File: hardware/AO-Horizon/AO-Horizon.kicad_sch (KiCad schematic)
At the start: 0 parts

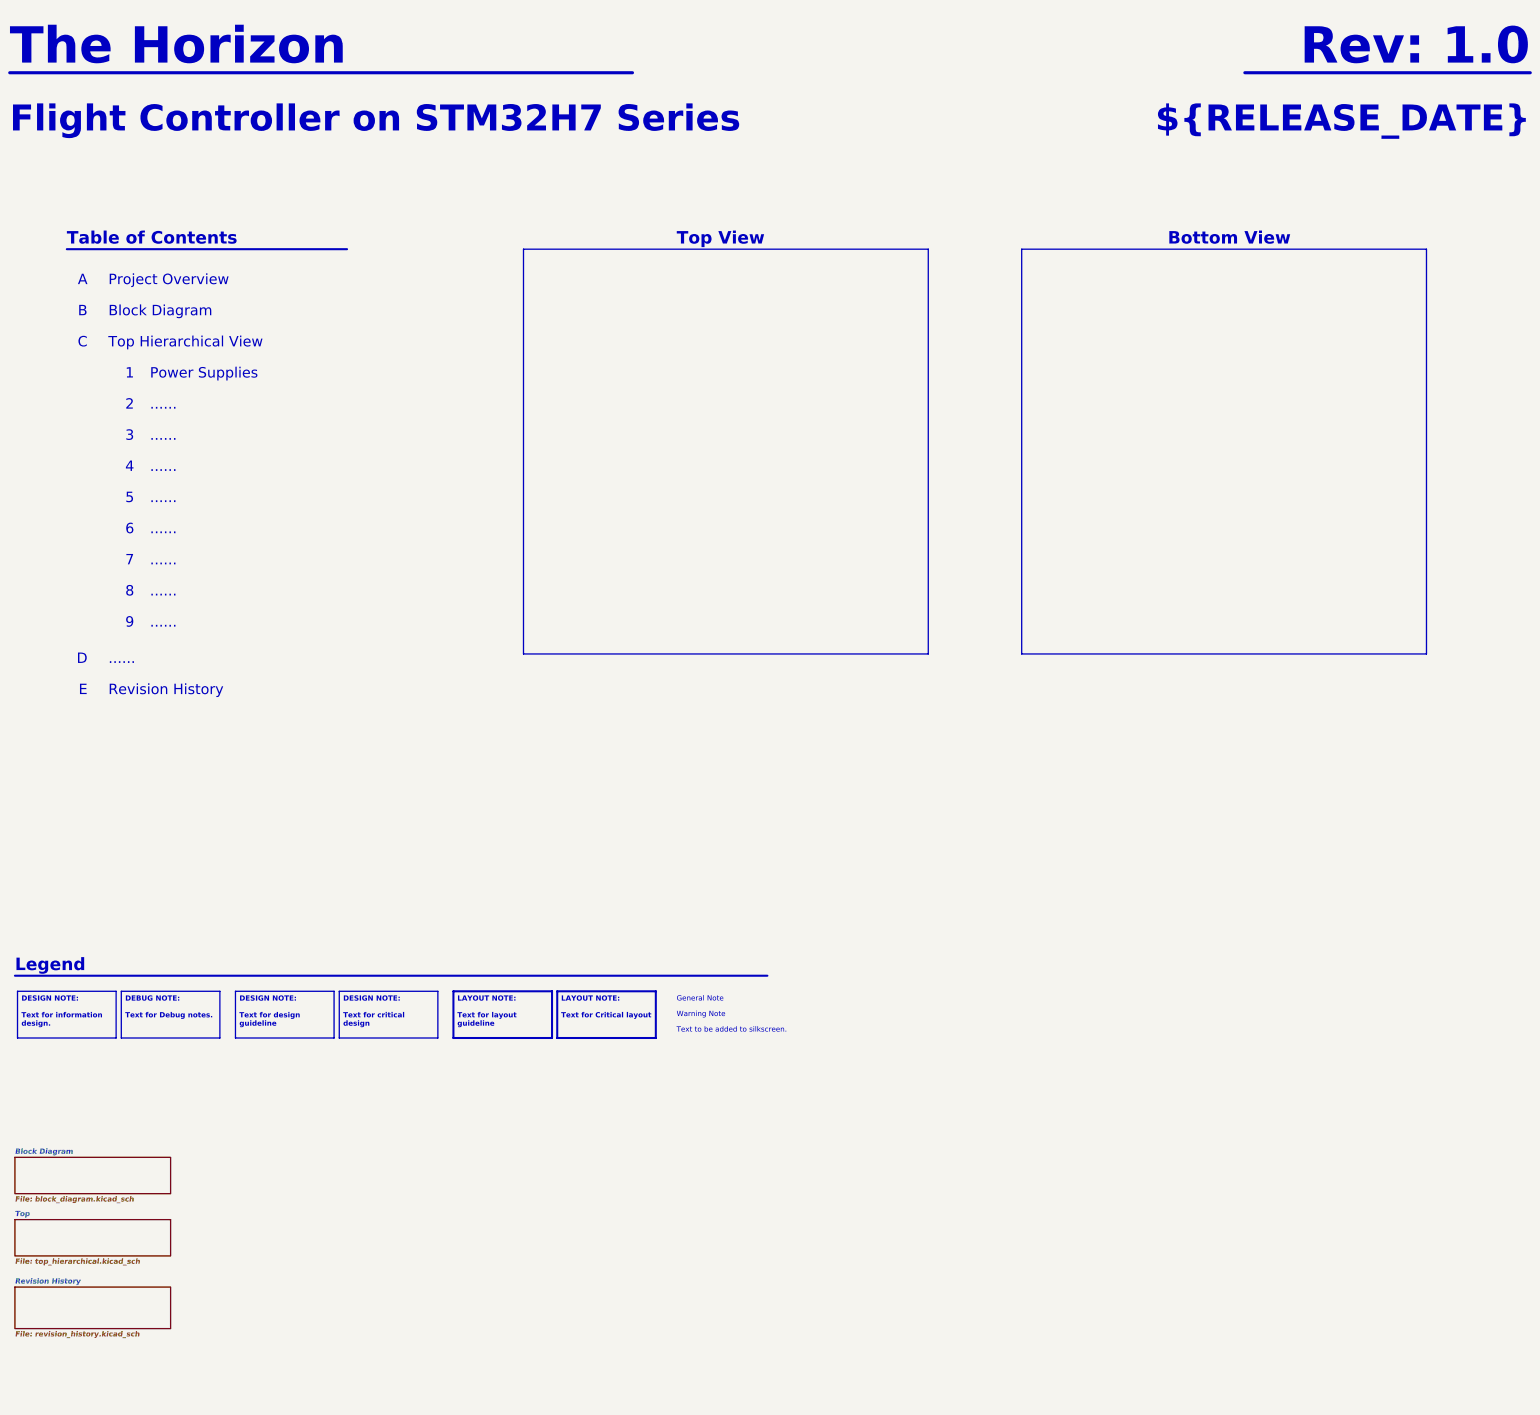
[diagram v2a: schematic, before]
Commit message: feat: close the power sheet capture (spec 0.19, DEC-027, DEC-028) (#31)
* docs(readme): simplify workflow diagram explanation

Mark DRAFT as under review, sync CHECK label, and add a colour key in README and template.

Co-Authored-By: Claude Sonnet 5.5 <noreply@anthropic.com>

* Update settings.json

* change spec file name

* update git-workflow skill

* change skill name by add hw-*

* docs: update AeroOptix-Horizon hardware spec

* docs: consolidate hardware handoff into checklist

* Update CLAUDE.md

* Update CLAUDE.md

* Update CLAUDE.md

* feat(hooks): replace protect hook with rule-based v2

Move file-protection rules into hooks/protect.json (allow > deny > ask)
and use ask for editable-with-approval files instead of a hard block.
Bash/PowerShell checks now inspect write targets, not any mention of a
protected path. Align settings.json permissions and drop the old hook.

Co-Authored-By: Claude Sonnet 5.5 <noreply@anthropic.com>

* docs: update CLAUDE.md for protection tiers and skill names

Describe the ask/deny protection rules, the v2 hook and protect.json,
and fix stale skill and template names.

Co-Authored-By: Claude Sonnet 5.5 <noreply@anthropic.com>

* Update .gitignore

* Update .gitignore

* Update .gitignore

* del skills

* Update engineering.md

* Update git-workflow.md

* Update hardware-workflow.md

* Update settings.json

* Update pull_request_template.md

* Update .gitignore

* Update .gitignore

* Delete SKILL.md

* Delete SKILL.md

* Update .gitignore

* add git-workflow skill

* Update CLAUDE.md

* Update protect.json

* Update settings.json

* Create MEMORY.md

* feat(agents): add codex-hw-delegate for bounded Codex tasks

Add a project agent that delegates one small, read-only-by-default task
to Codex CLI. It gates trivial or ambiguous requests, refuses PDF and
KiCad file contents, never mutates git, cross-checks Codex output and
returns a fixed report format.

Co-Authored-By: Claude Sonnet 5.5 <noreply@anthropic.com>

* fix(hooks): resol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
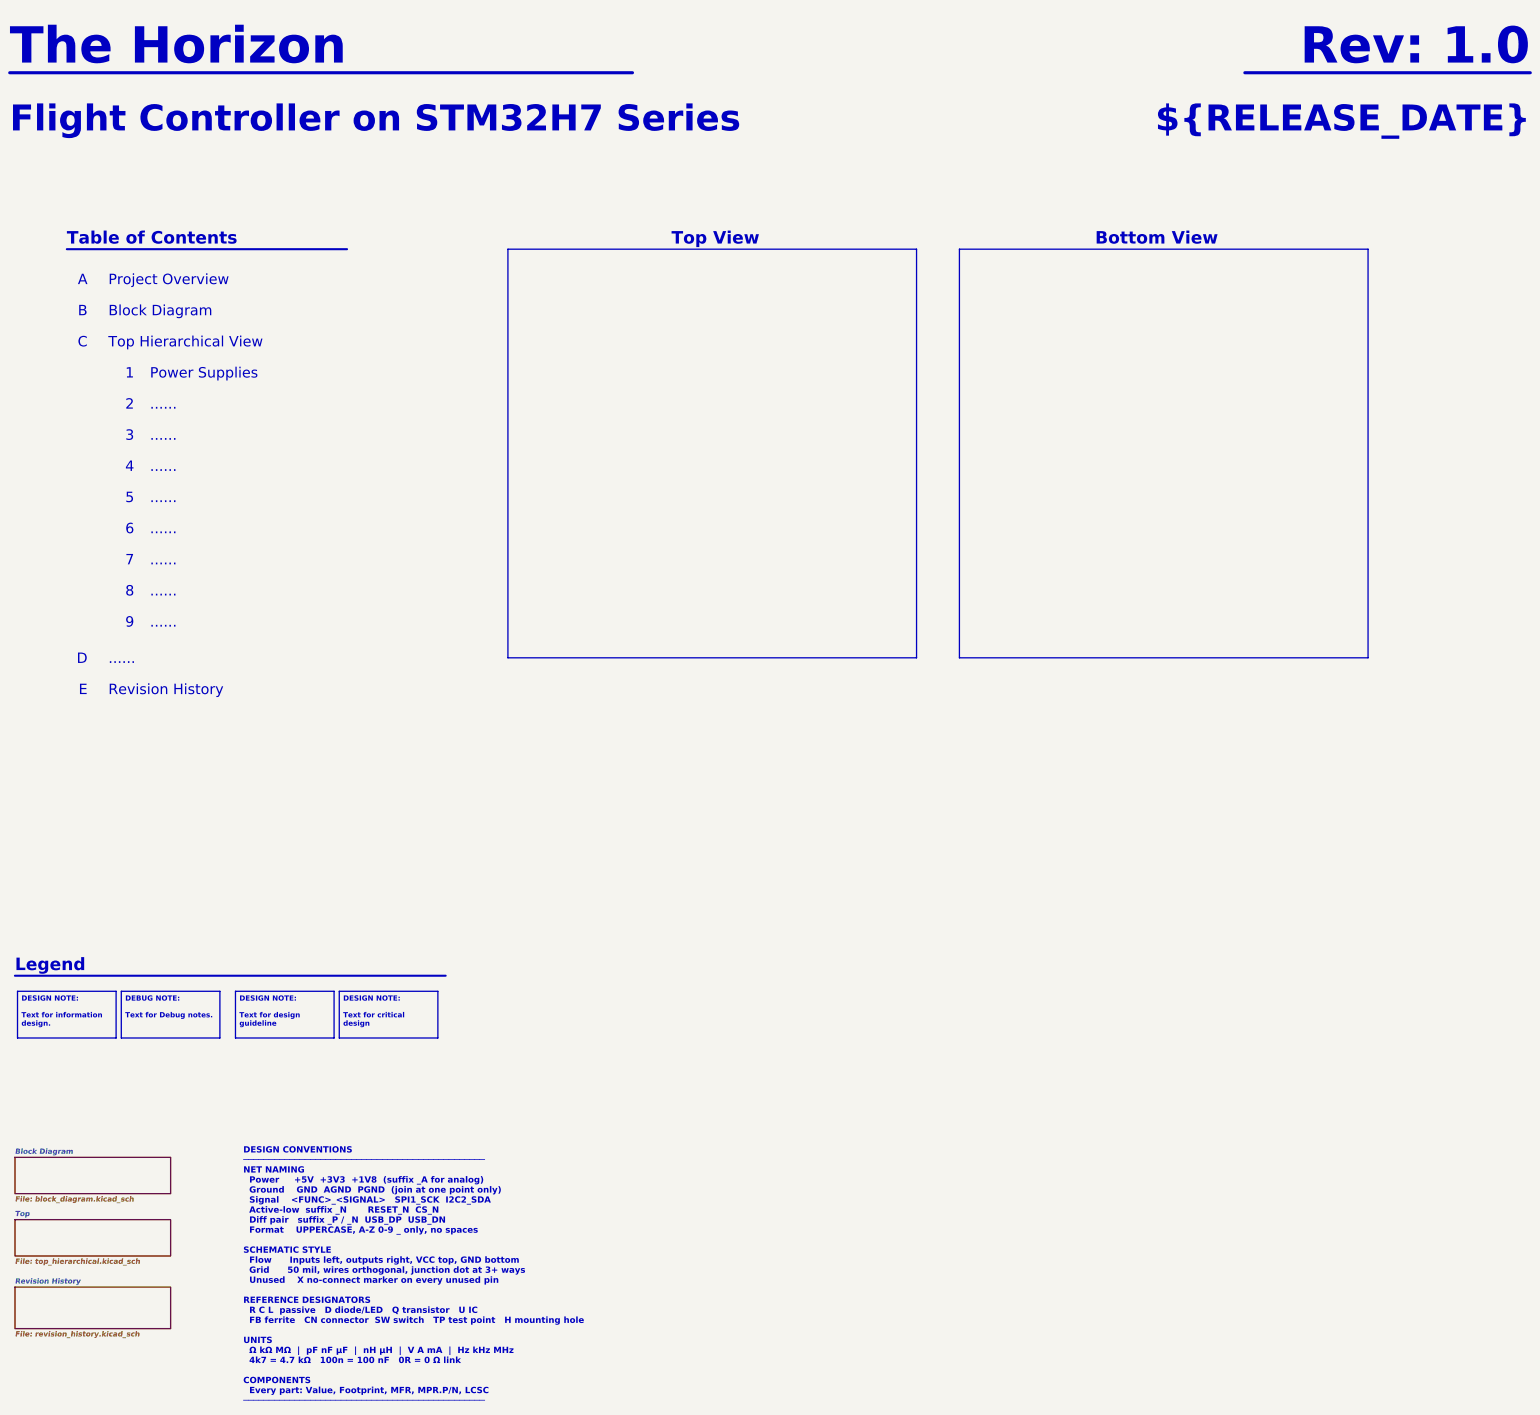
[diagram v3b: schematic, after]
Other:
- note added: "DESIGN CONVENTIONS ─────────────────────────────────────────────── NET NAMING Power +5V +3V3 +1V8 (suffix _A for analog) Ground GND AGND PGND (join at one point only) Signal <FUNC>_<SIGNAL> SPI1_SCK I2C2_SDA Active-low suffix _N RESET_N CS_N Diff pair suffix _P / _N USB_DP USB_DN Format UPPERCASE, A-Z 0-9 _ only, no spaces SCHEMATIC STYLE Flow Inputs left, outputs right, VCC top, GND bottom Grid 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"
- note removed: "General Note"
- note removed: "Text to be added to silkscreen."
- note removed: "Warning Note"
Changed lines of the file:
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@@
 	)
 	(rectangle
-		(start 151.13 83.82)
-		(end 250.19 182.88)
+		(start 147.32 83.82)
+		(end 247.32 183.82)
 		(stroke
 			(width 0)
@@
 	)
 	(rectangle
-		(start 273.05 83.82)
-		(end 372.11 182.88)
+		(start 257.81 83.82)
+		(end 357.81 183.82)
 		(stroke
 			(width 0)
@@
 		)
 	)
+	(text "DESIGN CONVENTIONS\n───────────────────────────────────────────────\nNET NAMING\n  Power     +5V  +3V3  +1V8  (suffix _A for analog)\n  Ground    GND  AGND  PGND  (join at one point only)\n  Signal    <FUNC>_<SIGNAL>   SPI1_SCK  I2C2_SDA\n  Active-low  suffix _N       RESET_N  CS_N\n  Diff pair   suffix _P / _N  USB_DP  USB_DN\n  Format    UPPERCASE, A-Z 0-9 _ only, no spaces\n\nSCHEMATIC STYLE\n  Flow      Inputs left, outputs right, VCC top, GND bottom\n  Grid      50 mil, wires orthogonal, junction dot at 3+ ways\n  Unused    X no-connect marker on every unused pin\n\nREFERENCE DESIGNATORS\n  R C L  passive   D diode/LED   Q transistor   U IC\n  FB ferrite   CN connector  SW switch   TP test point   H mounting hole\n\nUNITS\n  Ω kΩ MΩ  |  pF nF µF  |  nH µH  |  V A mA  |  Hz kHz MHz\n  4k7 = 4.7 kΩ   100n = 100 nF   0R = 0 Ω link\n\nCOMPONENTS\n  Every part: Value, Footprint, MFR, MPR.P/N, LCSC\n───────────────────────────────────────────────"
+		(exclude_from_sim no)
+		(at 82.55 303.53 0)
+		(effects
+			(font
+				(face "Century Gothic")
+				(size 1.524 1.524)
+				(bold yes)
+			)
+			(justify left top)
+		)
+	)
 	(text "......"
 		(exclude_from_sim no)
@@
 		)
 	)
-	(text "General Note"
-		(exclude_from_sim no)
-		(at 188.595 267.335 0)
-		(effects
-			(font
-				(size 1.27 1.27)
-				(color 0 0 194 1)
-			)
-			(justify left)
-		)
-	)
 	(text "Project Overview"
 		(exclude_from_sim no)
@@
 		)
 	)
-	(text "Text to be added to silkscreen."
-		(exclude_from_sim no)
-		(at 188.595 274.955 0)
-		(effects
-			(font
-				(size 1.27 1.27)
-				(color 0 132 132 1)
-			)
-			(justify left)
-		)
-	)
 	(text "6"
 		(exclude_from_sim no)
@@
 		)
 	)
-	(text "Warning Note"
-		(exclude_from_sim no)
-		(at 188.595 271.145 0)
-		(effects
-			(font
-				(size 1.27 1.27)
-				(color 194 0 0 1)
-			)
-			(justify left)
-		)
-	)
 	(text "Table of Contents"
 		(exclude_from_sim no)
@@
 	(text "Bottom View"
 		(exclude_from_sim no)
-		(at 323.85 81.28 0)
+		(at 306.07 81.28 0)
 		(effects
 			(font
@@
 	(text "Top View"
 		(exclude_from_sim no)
-		(at 199.39 81.28 0)
+		(at 198.12 81.28 0)
 		(effects
 			(font
@@
 		)
 	)
-	(text_box "LAYOUT NOTE:\n\nText for layout guideline\n\n"
-		(exclude_from_sim no)
-		(at 133.985 265.43 0)
-		(size 24.13 11.43)
-		(margins 0.9525 0.9525 0.9525 0.9525)
-		(stroke
-			(width 0.5)
-			(type solid)
-			(color 0 0 194 1)
-		)
-		(fill
-			(type color)
-			(color 255 255 194 1)
-		)
-		(effects
-			(font
-				(face "Century Gothic")
-				(size 1.27 1.27)
-				(thickness 0.1588)
-				(bold yes)
-				(color 0 0 194 1)
-			)
-			(justify left top)
-		)
-	)
 	(text_box "DEBUG NOTE:\n\nText for Debug notes.\n"
 		(exclude_from_sim no)
@@
 		)
 	)
-	(text_box "LAYOUT NOTE:\n\nText for Critical layout"
-		(exclude_from_sim no)
-		(at 159.385 265.43 0)
-		(size 24.13 11.43)
-		(margins 0.9525 0.9525 0.9525 0.9525)
-		(stroke
-			(width 0.5)
-			(type solid)
-			(color 255 0 0 1)
-		)
-		(fill
-			(type color)
-			(color 255 255 194 1)
-		)
-		(effects
-			(font
-				(face "Century Gothic")
-				(size 1.27 1.27)
-				(thickness 0.1588)
-				(bold yes)
-				(color 194 0 0 1)
-			)
-			(justify left top)
-		)
-	)
 	(text_box "DESIGN NOTE:\n\nText for design guideline\n\n"
 		(exclude_from_sim no)
@@
 	(polyline
 		(pts
-			(xy 26.67 261.62) (xy 210.82 261.62)
-		)
-		(stroke
+			(xy 26.67 261.62) (xy 132.08 261.62)
+		)
+		(stroke
